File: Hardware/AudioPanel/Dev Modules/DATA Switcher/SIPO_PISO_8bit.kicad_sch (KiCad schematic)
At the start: 5 parts, among them U1001 SN74LV165ARGYR, U601 SN74LV595ARGYR

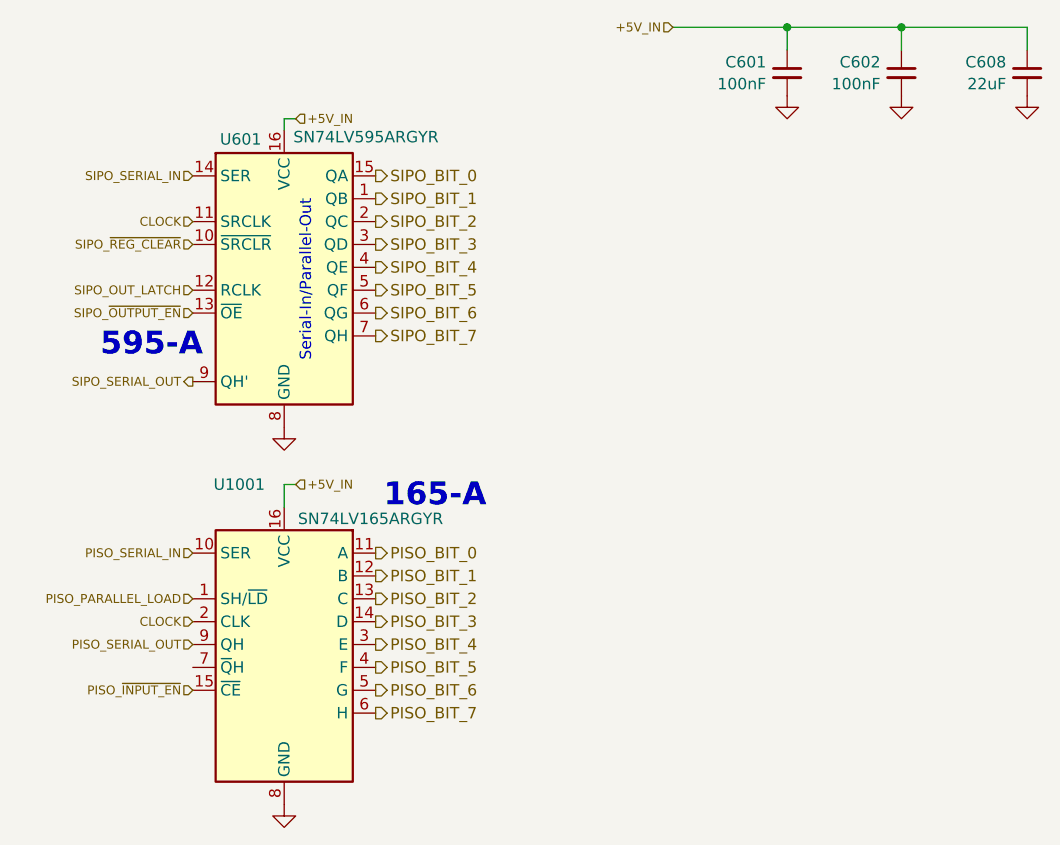
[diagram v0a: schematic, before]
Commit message: Adjusted I2C addresses and component identifiers
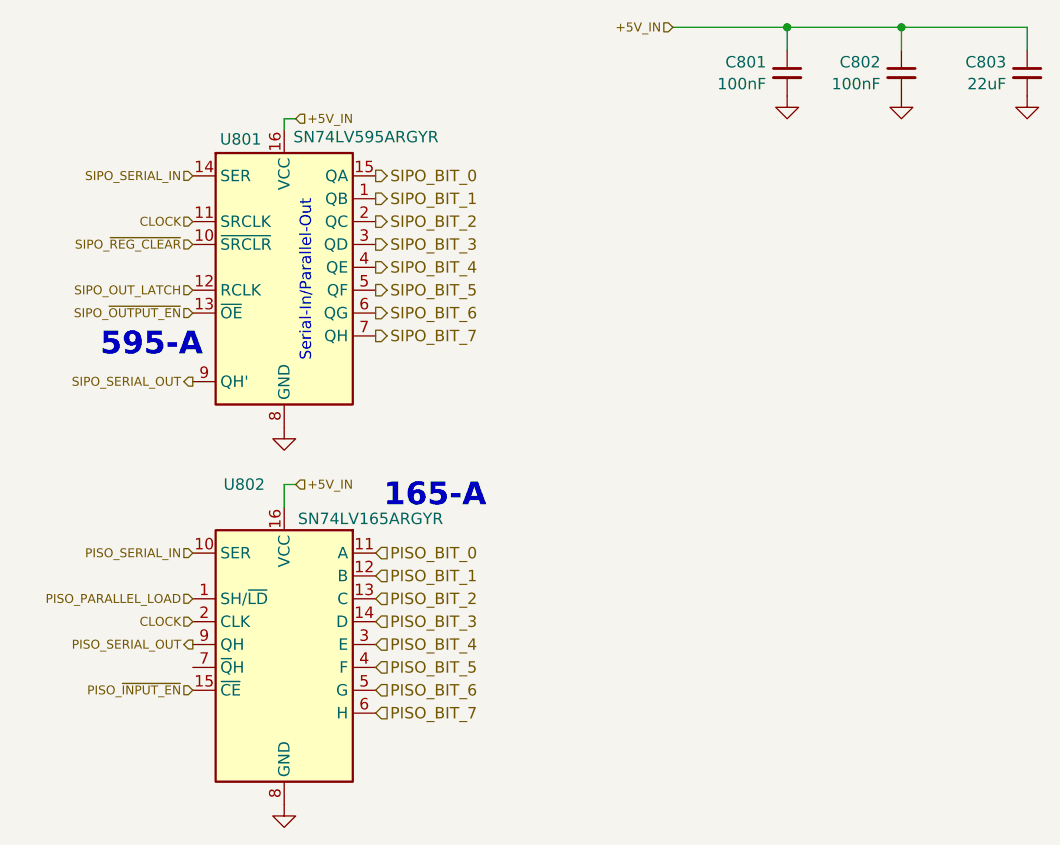
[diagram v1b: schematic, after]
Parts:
- renumbered C601 to C801, C602 to C802, C608 to C803, U601 to U801, U1001 to U802
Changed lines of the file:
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@@
 	)
 	(hierarchical_label "PISO_BIT_7"
-		(shape output)
+		(shape input)
 		(at 163.83 153.67 0)
 		(effects
@@
 	)
 	(hierarchical_label "PISO_BIT_1"
-		(shape output)
+		(shape input)
 		(at 163.83 138.43 0)
 		(effects
@@
 	)
 	(hierarchical_label "PISO_BIT_4"
-		(shape output)
+		(shape input)
 		(at 163.83 146.05 0)
 		(effects
@@
 	)
 	(hierarchical_label "PISO_BIT_0"
-		(shape output)
+		(shape input)
 		(at 163.83 135.89 0)
 		(effects
@@
 	)
 	(hierarchical_label "PISO_BIT_2"
-		(shape output)
+		(shape input)
 		(at 163.83 140.97 0)
 		(effects
@@
 	)
 	(hierarchical_label "PISO_SERIAL_OUT"
-		(shape input)
+		(shape output)
 		(at 143.51 146.05 180)
 		(effects
@@
 	)
 	(hierarchical_label "PISO_BIT_5"
-		(shape output)
+		(shape input)
 		(at 163.83 148.59 0)
 		(effects
@@
 	)
 	(hierarchical_label "PISO_BIT_6"
-		(shape output)
+		(shape input)
 		(at 163.83 151.13 0)
 		(effects
@@
 	)
 	(hierarchical_label "PISO_BIT_3"
-		(shape output)
+		(shape input)
 		(at 163.83 143.51 0)
 		(effects
@@
 		(on_board yes)
 		(dnp no)
-		(property "Reference" "C608"
+		(property "Reference" "C803"
 			(at 233.8959 81.3441 0)
 			(effects
@@
 			(project "DATA Switcher"
 				(path "/f4364825-c4d0-42ed-9bb3-69baf38bc2d0/40c58ec3-1e61-4d0e-9eb6-78add36d507c"
-					(reference "C608")
+					(reference "C803")
 					(unit 1)
 				)
@@
 		(dnp no)
 		(fields_autoplaced yes)
-		(property "Reference" "#PWR0601"
+		(property "Reference" "#PWR0804"
 			(at 153.67 128.27 0)
 			(effects
@@
 			(project "DATA Switcher"
 				(path "/f4364825-c4d0-42ed-9bb3-69baf38bc2d0/40c58ec3-1e61-4d0e-9eb6-78add36d507c"
-					(reference "#PWR0601")
+					(reference "#PWR0804")
 					(unit 1)
 				)
@@
 		(dnp no)
 		(fields_autoplaced yes)
-		(property "Reference" "#PWR0614"
+		(property "Reference" "#PWR0803"
 			(at 236.22 91.44 0)
 			(effects
@@
 			(project "DATA Switcher"
 				(path "/f4364825-c4d0-42ed-9bb3-69baf38bc2d0/40c58ec3-1e61-4d0e-9eb6-78add36d507c"
-					(reference "#PWR0614")
+					(reference "#PWR0803")
 					(unit 1)
 				)
@@
 		(dnp no)
 		(fields_autoplaced yes)
-		(property "Reference" "#PWR0608"
+		(property "Reference" "#PWR0802"
 			(at 222.25 91.44 0)
 			(effects
@@
 			(project "DATA Switcher"
 				(path "/f4364825-c4d0-42ed-9bb3-69baf38bc2d0/40c58ec3-1e61-4d0e-9eb6-78add36d507c"
-					(reference "#PWR0608")
+					(reference "#PWR0802")
 					(unit 1)
 				)
@@
 		(dnp no)
 		(fields_autoplaced yes)
-		(property "Reference" "#PWR0607"
+		(property "Reference" "#PWR0801"
 			(at 209.55 91.44 0)
 			(effects
@@
 			(project "DATA Switcher"
 				(path "/f4364825-c4d0-42ed-9bb3-69baf38bc2d0/40c58ec3-1e61-4d0e-9eb6-78add36d507c"
-					(reference "#PWR0607")
+					(reference "#PWR0801")
 					(unit 1)
 				)
@@
 		(on_board yes)
 		(dnp no)
-		(property "Reference" "U601"
+		(property "Reference" "U801"
 			(at 151.13 89.916 0)
 			(effects
@@
 			(project "DATA Switcher"
 				(path "/f4364825-c4d0-42ed-9bb3-69baf38bc2d0/40c58ec3-1e61-4d0e-9eb6-78add36d507c"
-					(reference "U601")
+					(reference "U801")
 					(unit 1)
 				)
@@
 		(on_board yes)
 		(dnp no)
-		(property "Reference" "C601"
+		(property "Reference" "C801"
 			(at 207.2259 81.3441 0)
 			(effects
@@
 			(project "DATA Switcher"
 				(path "/f4364825-c4d0-42ed-9bb3-69baf38bc2d0/40c58ec3-1e61-4d0e-9eb6-78add36d507c"
-					(reference "C601")
+					(reference "C801")
 					(unit 1)
 				)
@@
 		(dnp no)
 		(fields_autoplaced yes)
-		(property "Reference" "#PWR01014"
+		(property "Reference" "#PWR0805"
 			(at 153.67 170.18 0)
 			(effects
@@
 			(project "DATA Switcher"
 				(path "/f4364825-c4d0-42ed-9bb3-69baf38bc2d0/40c58ec3-1e61-4d0e-9eb6-78add36d507c"
-					(reference "#PWR01014")
+					(reference "#PWR0805")
 					(unit 1)
 				)
@@
 		(on_board yes)
 		(dnp no)
-		(property "Reference" "C602"
+		(property "Reference" "C802"
 			(at 219.9259 81.3441 0)
 			(effects
@@
 			(project "DATA Switcher"
 				(path "/f4364825-c4d0-42ed-9bb3-69baf38bc2d0/40c58ec3-1e61-4d0e-9eb6-78add36d507c"
-					(reference "C602")
+					(reference "C802")
 					(unit 1)
 				)
@@
 		(on_board yes)
 		(dnp no)
-		(property "Reference" "U1001"
+		(property "Reference" "U802"
 			(at 151.5267 128.27 0)
 			(effects
@@
 			(project "DATA Switcher"
 				(path "/f4364825-c4d0-42ed-9bb3-69baf38bc2d0/40c58ec3-1e61-4d0e-9eb6-78add36d507c"
-					(reference "U1001")
+					(reference "U802")
 					(unit 1)
 				)

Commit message: DATA switcher put together
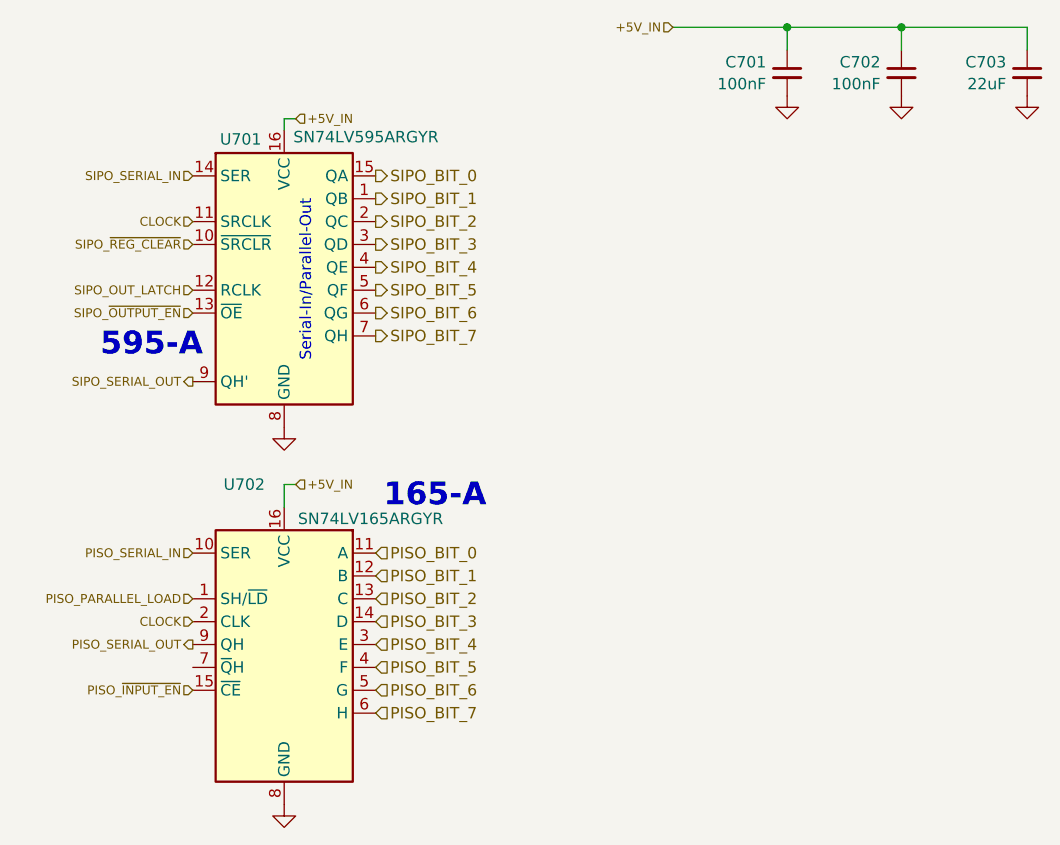
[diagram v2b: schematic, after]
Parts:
- renumbered C801 to C701, C802 to C702, C803 to C703, U801 to U701, U802 to U702
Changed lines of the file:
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@@
 		(on_board yes)
 		(dnp no)
-		(property "Reference" "C803"
+		(property "Reference" "C703"
 			(at 233.8959 81.3441 0)
 			(effects
@@
 			(project "DATA Switcher"
 				(path "/f4364825-c4d0-42ed-9bb3-69baf38bc2d0/40c58ec3-1e61-4d0e-9eb6-78add36d507c"
-					(reference "C803")
+					(reference "C703")
 					(unit 1)
 				)
@@
 		(dnp no)
 		(fields_autoplaced yes)
-		(property "Reference" "#PWR0804"
+		(property "Reference" "#PWR0704"
 			(at 153.67 128.27 0)
 			(effects
@@
 			(project "DATA Switcher"
 				(path "/f4364825-c4d0-42ed-9bb3-69baf38bc2d0/40c58ec3-1e61-4d0e-9eb6-78add36d507c"
-					(reference "#PWR0804")
+					(reference "#PWR0704")
 					(unit 1)
 				)
@@
 		(dnp no)
 		(fields_autoplaced yes)
-		(property "Reference" "#PWR0803"
+		(property "Reference" "#PWR0703"
 			(at 236.22 91.44 0)
 			(effects
@@
 			(project "DATA Switcher"
 				(path "/f4364825-c4d0-42ed-9bb3-69baf38bc2d0/40c58ec3-1e61-4d0e-9eb6-78add36d507c"
-					(reference "#PWR0803")
+					(reference "#PWR0703")
 					(unit 1)
 				)
@@
 		(dnp no)
 		(fields_autoplaced yes)
-		(property "Reference" "#PWR0802"
+		(property "Reference" "#PWR0702"
 			(at 222.25 91.44 0)
 			(effects
@@
 			(project "DATA Switcher"
 				(path "/f4364825-c4d0-42ed-9bb3-69baf38bc2d0/40c58ec3-1e61-4d0e-9eb6-78add36d507c"
-					(reference "#PWR0802")
+					(reference "#PWR0702")
 					(unit 1)
 				)
@@
 		(dnp no)
 		(fields_autoplaced yes)
-		(property "Reference" "#PWR0801"
+		(property "Reference" "#PWR0701"
 			(at 209.55 91.44 0)
 			(effects
@@
 			(project "DATA Switcher"
 				(path "/f4364825-c4d0-42ed-9bb3-69baf38bc2d0/40c58ec3-1e61-4d0e-9eb6-78add36d507c"
-					(reference "#PWR0801")
+					(reference "#PWR0701")
 					(unit 1)
 				)
@@
 		(on_board yes)
 		(dnp no)
-		(property "Reference" "U801"
+		(property "Reference" "U701"
 			(at 151.13 89.916 0)
 			(effects
@@
 			(project "DATA Switcher"
 				(path "/f4364825-c4d0-42ed-9bb3-69baf38bc2d0/40c58ec3-1e61-4d0e-9eb6-78add36d507c"
-					(reference "U801")
+					(reference "U701")
 					(unit 1)
 				)
@@
 		(on_board yes)
 		(dnp no)
-		(property "Reference" "C801"
+		(property "Reference" "C701"
 			(at 207.2259 81.3441 0)
 			(effects
@@
 			(project "DATA Switcher"
 				(path "/f4364825-c4d0-42ed-9bb3-69baf38bc2d0/40c58ec3-1e61-4d0e-9eb6-78add36d507c"
-					(reference "C801")
+					(reference "C701")
 					(unit 1)
 				)
@@
 		(dnp no)
 		(fields_autoplaced yes)
-		(property "Reference" "#PWR0805"
+		(property "Reference" "#PWR0705"
 			(at 153.67 170.18 0)
 			(effects
@@
 			(project "DATA Switcher"
 				(path "/f4364825-c4d0-42ed-9bb3-69baf38bc2d0/40c58ec3-1e61-4d0e-9eb6-78add36d507c"
-					(reference "#PWR0805")
+					(reference "#PWR0705")
 					(unit 1)
 				)
@@
 		(on_board yes)
 		(dnp no)
-		(property "Reference" "C802"
+		(property "Reference" "C702"
 			(at 219.9259 81.3441 0)
 			(effects
@@
 			(project "DATA Switcher"
 				(path "/f4364825-c4d0-42ed-9bb3-69baf38bc2d0/40c58ec3-1e61-4d0e-9eb6-78add36d507c"
-					(reference "C802")
+					(reference "C702")
 					(unit 1)
 				)
@@
 		(on_board yes)
 		(dnp no)
-		(property "Reference" "U802"
+		(property "Reference" "U702"
 			(at 151.5267 128.27 0)
 			(effects
@@
 			(project "DATA Switcher"
 				(path "/f4364825-c4d0-42ed-9bb3-69baf38bc2d0/40c58ec3-1e61-4d0e-9eb6-78add36d507c"
-					(reference "U802")
-					(unit 1)
-				)
+					(reference "U702")
+					(unit 1)
+				)

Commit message: Many tweaks
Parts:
- renumbered C701 to C601, C702 to C602, C703 to C603, U701 to U601, U702 to U602
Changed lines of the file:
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@@
 		(on_board yes)
 		(dnp no)
-		(property "Reference" "C703"
+		(property "Reference" "C603"
 			(at 233.8959 81.3441 0)
 			(effects
@@
 			(project "DATA Switcher"
 				(path "/f4364825-c4d0-42ed-9bb3-69baf38bc2d0/40c58ec3-1e61-4d0e-9eb6-78add36d507c"
-					(reference "C703")
+					(reference "C603")
 					(unit 1)
 				)
@@
 		(dnp no)
 		(fields_autoplaced yes)
-		(property "Reference" "#PWR0704"
+		(property "Reference" "#PWR0604"
 			(at 153.67 128.27 0)
 			(effects
@@
 			(project "DATA Switcher"
 				(path "/f4364825-c4d0-42ed-9bb3-69baf38bc2d0/40c58ec3-1e61-4d0e-9eb6-78add36d507c"
-					(reference "#PWR0704")
+					(reference "#PWR0604")
 					(unit 1)
 				)
@@
 		(dnp no)
 		(fields_autoplaced yes)
-		(property "Reference" "#PWR0703"
+		(property "Reference" "#PWR0603"
 			(at 236.22 91.44 0)
 			(effects
@@
 			(project "DATA Switcher"
 				(path "/f4364825-c4d0-42ed-9bb3-69baf38bc2d0/40c58ec3-1e61-4d0e-9eb6-78add36d507c"
-					(reference "#PWR0703")
+					(reference "#PWR0603")
 					(unit 1)
 				)
@@
 		(dnp no)
 		(fields_autoplaced yes)
-		(property "Reference" "#PWR0702"
+		(property "Reference" "#PWR0602"
 			(at 222.25 91.44 0)
 			(effects
@@
 			(project "DATA Switcher"
 				(path "/f4364825-c4d0-42ed-9bb3-69baf38bc2d0/40c58ec3-1e61-4d0e-9eb6-78add36d507c"
-					(reference "#PWR0702")
+					(reference "#PWR0602")
 					(unit 1)
 				)
@@
 		(dnp no)
 		(fields_autoplaced yes)
-		(property "Reference" "#PWR0701"
+		(property "Reference" "#PWR0601"
 			(at 209.55 91.44 0)
 			(effects
@@
 			(project "DATA Switcher"
 				(path "/f4364825-c4d0-42ed-9bb3-69baf38bc2d0/40c58ec3-1e61-4d0e-9eb6-78add36d507c"
-					(reference "#PWR0701")
+					(reference "#PWR0601")
 					(unit 1)
 				)
@@
 		(on_board yes)
 		(dnp no)
-		(property "Reference" "U701"
+		(property "Reference" "U601"
 			(at 151.13 89.916 0)
 			(effects
@@
 			(project "DATA Switcher"
 				(path "/f4364825-c4d0-42ed-9bb3-69baf38bc2d0/40c58ec3-1e61-4d0e-9eb6-78add36d507c"
-					(reference "U701")
+					(reference "U601")
 					(unit 1)
 				)
@@
 		(on_board yes)
 		(dnp no)
-		(property "Reference" "C701"
+		(property "Reference" "C601"
 			(at 207.2259 81.3441 0)
 			(effects
@@
 			(project "DATA Switcher"
 				(path "/f4364825-c4d0-42ed-9bb3-69baf38bc2d0/40c58ec3-1e61-4d0e-9eb6-78add36d507c"
-					(reference "C701")
+					(reference "C601")
 					(unit 1)
 				)
@@
 		(dnp no)
 		(fields_autoplaced yes)
-		(property "Reference" "#PWR0705"
+		(property "Reference" "#PWR0605"
 			(at 153.67 170.18 0)
 			(effects
@@
 			(project "DATA Switcher"
 				(path "/f4364825-c4d0-42ed-9bb3-69baf38bc2d0/40c58ec3-1e61-4d0e-9eb6-78add36d507c"
-					(reference "#PWR0705")
+					(reference "#PWR0605")
 					(unit 1)
 				)
@@
 		(on_board yes)
 		(dnp no)
-		(property "Reference" "C702"
+		(property "Reference" "C602"
 			(at 219.9259 81.3441 0)
 			(effects
@@
 			(project "DATA Switcher"
 				(path "/f4364825-c4d0-42ed-9bb3-69baf38bc2d0/40c58ec3-1e61-4d0e-9eb6-78add36d507c"
-					(reference "C702")
+					(reference "C602")
 					(unit 1)
 				)
@@
 		(on_board yes)
 		(dnp no)
-		(property "Reference" "U702"
+		(property "Reference" "U602"
 			(at 151.5267 128.27 0)
 			(effects
@@
 			(project "DATA Switcher"
 				(path "/f4364825-c4d0-42ed-9bb3-69baf38bc2d0/40c58ec3-1e61-4d0e-9eb6-78add36d507c"
-					(reference "U702")
-					(unit 1)
-				)
+					(reference "U602")
+					(unit 1)
+				)
